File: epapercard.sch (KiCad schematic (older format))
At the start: 47 parts, among them P1 CONN_01X06, P2 A120699CT, Q1 2N7002KW, Q2 BSS84W, Q3 BSS84W, Q4 BSS84W, Q5 2N7002KW, Q6 2N7002KW, Q7 2N7002KW, SW1 SW_PUSH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

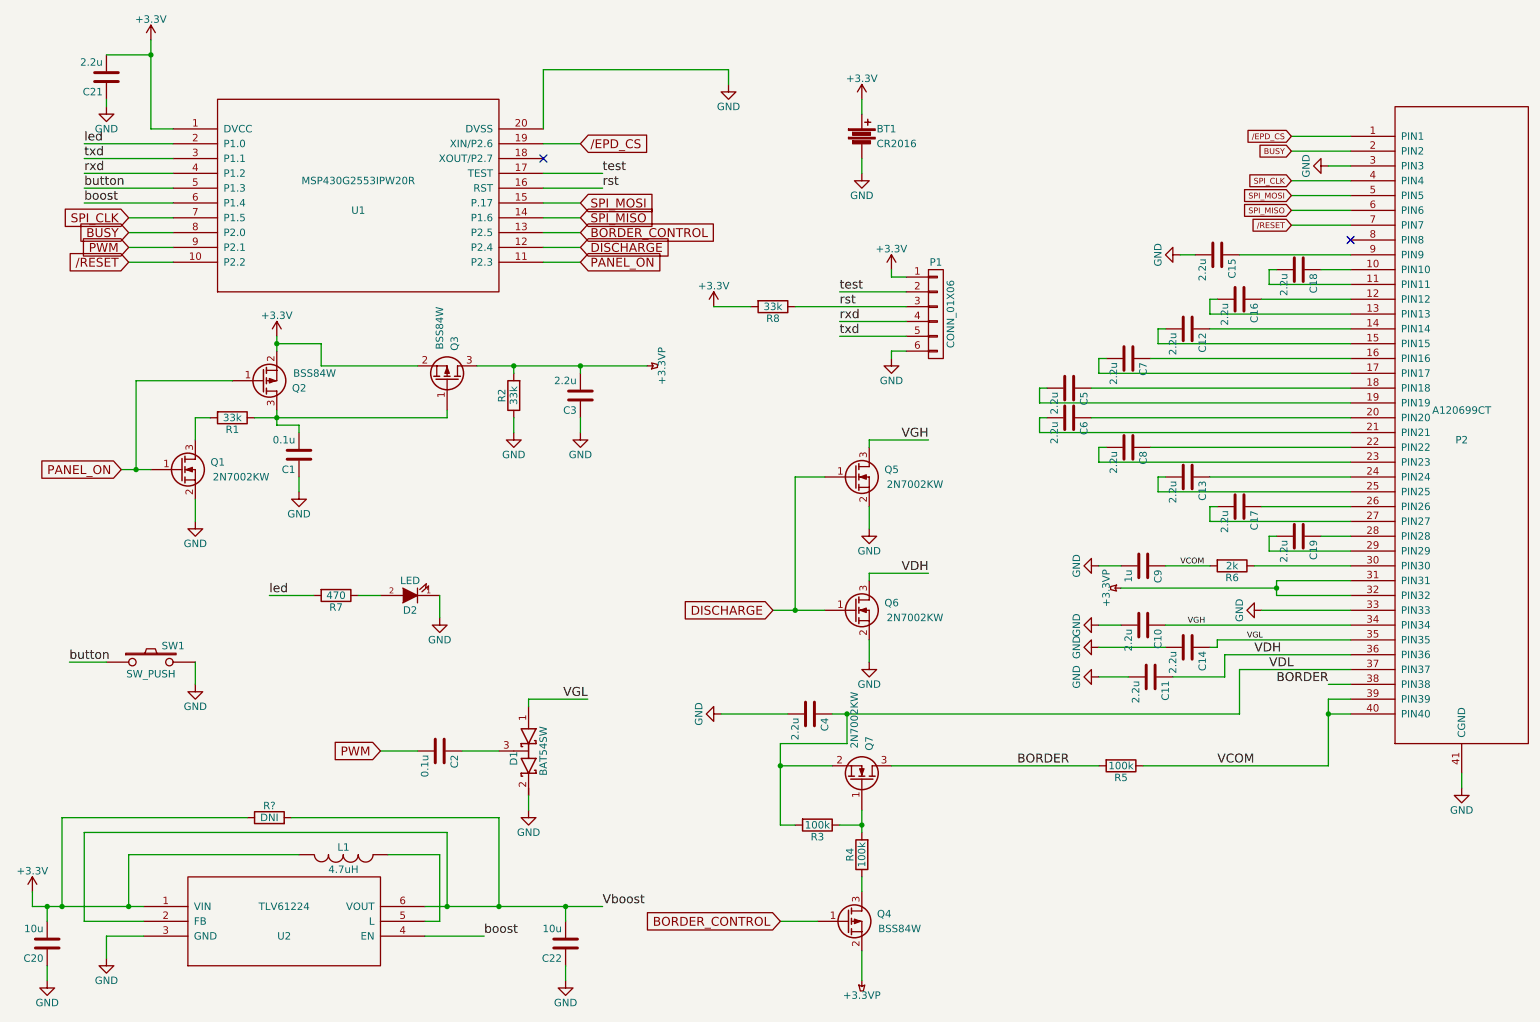
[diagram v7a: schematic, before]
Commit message: Add tabbed battery and boost reg
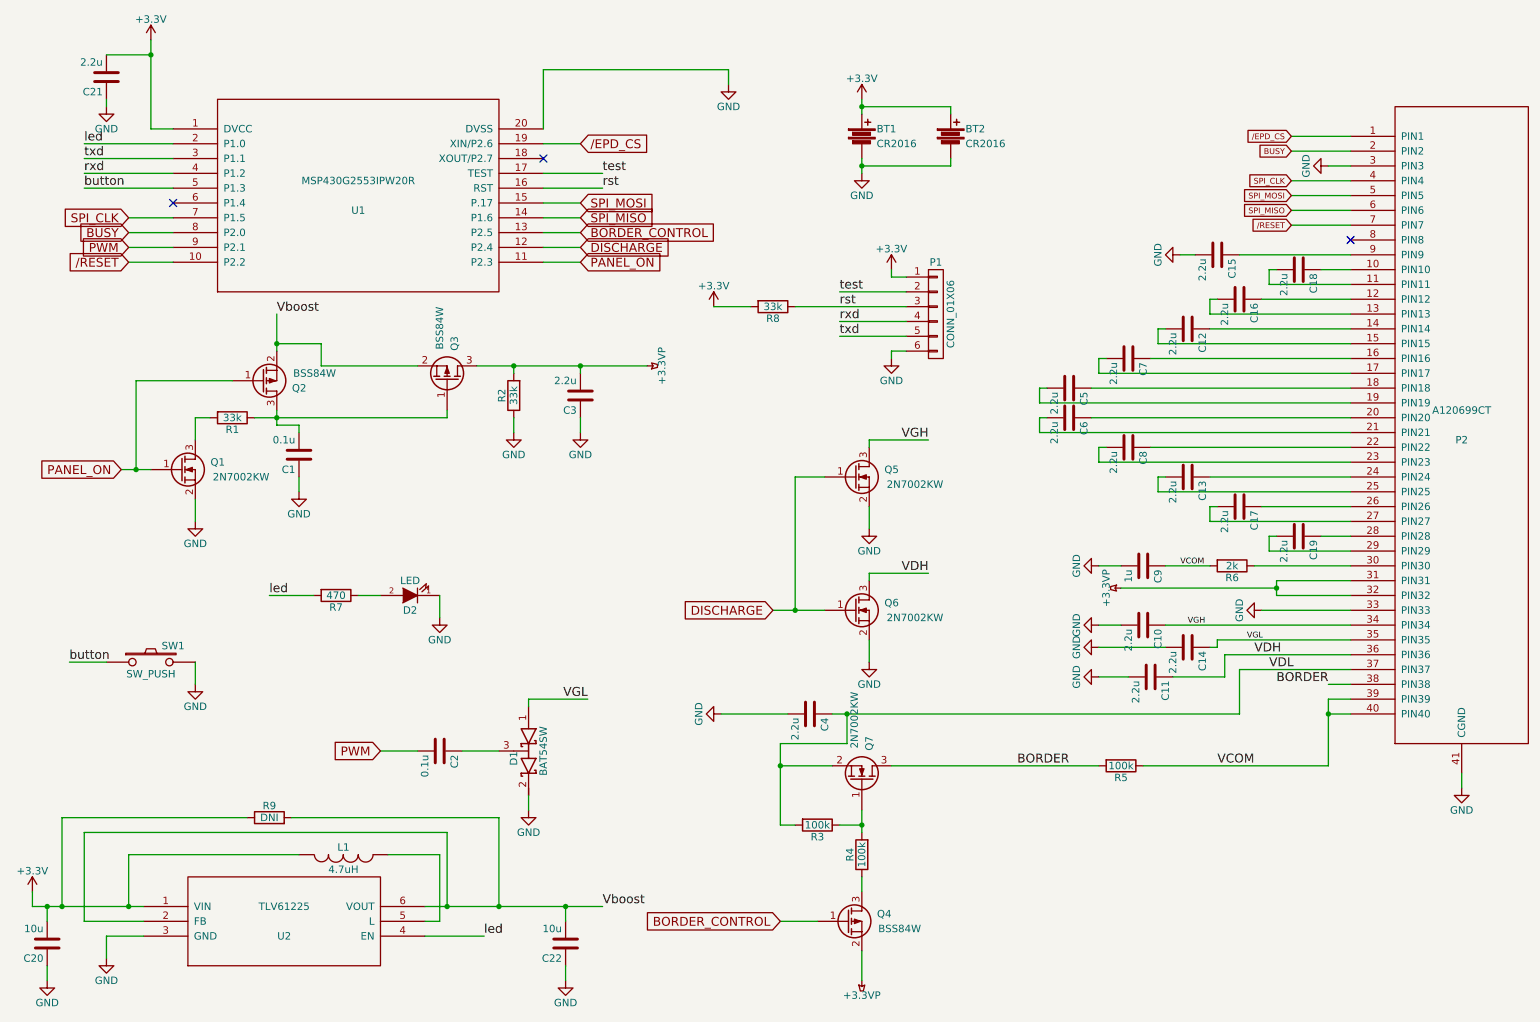
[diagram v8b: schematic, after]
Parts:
- added BT2: CR2016, footprint:CR2032sm, symbol Battery
- BT1: footprint footprint:CR2016sm -> footprint:CR2016sm-F2N
- U2: value TLV61224 -> TLV61225
- gave numbers to parts that had none: 1
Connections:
- net +3V3: now also BT2.1; no longer Q2.2 (S), Q3.2 (S)
- net GND: now also BT2.2
- net Vboost: now also Q2.2 (S), Q3.2 (S)
- net led: now also U2.4 (EN)
- net boost: no longer names the net of U1.6 (P1.4)
- net boost: no longer U2.4 (EN)
- no-connect marks 2 -> 3
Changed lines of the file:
@@
 $EndComp
 $Comp
-L +3.3V #PWR5
+L +3.3V #PWR01
 U 1 1 5733FF8C
 P 1550 700
-F 0 "#PWR5" H 1550 550 50  0001 C CNN
+F 0 "#PWR01" H 1550 550 50  0001 C CNN
 F 1 "+3.3V" H 1550 840 50  0000 C CNN
 F 2 "" H 1550 700 50  0000 C CNN
@@
 $EndComp
 $Comp
-L GND #PWR18
+L GND #PWR02
 U 1 1 5733FFAC
 P 5450 1000
-F 0 "#PWR18" H 5450 750 50  0001 C CNN
+F 0 "#PWR02" H 5450 750 50  0001 C CNN
 F 1 "GND" H 5450 850 50  0000 C CNN
 F 2 "" H 5450 1000 50  0000 C CNN
@@
 $EndComp
 $Comp
-L GND #PWR34
+L GND #PWR03
 U 1 1 57340122
 P 10400 5750
-F 0 "#PWR34" H 10400 5500 50  0001 C CNN
+F 0 "#PWR03" H 10400 5500 50  0001 C CNN
 F 1 "GND" H 10400 5600 50  0000 C CNN
 F 2 "" H 10400 5750 50  0000 C CNN
@@
 BUSY
 $Comp
-L GND #PWR33
+L GND #PWR04
 U 1 1 573405DC
 P 9500 1550
-F 0 "#PWR33" H 9500 1300 50  0001 C CNN
+F 0 "#PWR04" H 9500 1300 50  0001 C CNN
 F 1 "GND" H 9500 1400 50  0000 C CNN
 F 2 "" H 9500 1550 50  0000 C CNN
@@
 $EndComp
 $Comp
-L GND #PWR31
+L GND #PWR05
 U 1 1 57340979
 P 8500 2150
-F 0 "#PWR31" H 8500 1900 50  0001 C CNN
+F 0 "#PWR05" H 8500 1900 50  0001 C CNN
 F 1 "GND" H 8500 2000 50  0000 C CNN
 F 2 "" H 8500 2150 50  0000 C CNN
@@
 $EndComp
 $Comp
-L GND #PWR26
+L GND #PWR06
 U 1 1 5734231E
 P 7950 4250
-F 0 "#PWR26" H 7950 4000 50  0001 C CNN
+F 0 "#PWR06" H 7950 4000 50  0001 C CNN
 F 1 "GND" H 7950 4100 50  0000 C CNN
 F 2 "" H 7950 4250 50  0000 C CNN
@@
 Connection ~ 9150 4400
 $Comp
-L GND #PWR32
+L GND #PWR07
 U 1 1 57342C10
 P 9050 4550
-F 0 "#PWR32" H 9050 4300 50  0001 C CNN
+F 0 "#PWR07" H 9050 4300 50  0001 C CNN
 F 1 "GND" H 9050 4400 50  0000 C CNN
 F 2 "" H 9050 4550 50  0000 C CNN
@@
 VGH
 $Comp
-L GND #PWR27
+L GND #PWR08
 U 1 1 57343007
 P 7950 4650
-F 0 "#PWR27" H 7950 4400 50  0001 C CNN
+F 0 "#PWR08" H 7950 4400 50  0001 C CNN
 F 1 "GND" H 7950 4500 50  0000 C CNN
 F 2 "" H 7950 4650 50  0000 C CNN
@@
 VGL
 $Comp
-L GND #PWR28
+L GND #PWR09
 U 1 1 573432AB
 P 7950 4800
-F 0 "#PWR28" H 7950 4550 50  0001 C CNN
+F 0 "#PWR09" H 7950 4550 50  0001 C CNN
 F 1 "GND" H 7950 4650 50  0000 C CNN
 F 2 "" H 7950 4800 50  0000 C CNN
@@
 	6400 4300 6800 4300
 $Comp
-L GND #PWR22
+L GND #PWR010
 U 1 1 57341714
 P 6400 4000
-F 0 "#PWR22" H 6400 3750 50  0001 C CNN
+F 0 "#PWR010" H 6400 3750 50  0001 C CNN
 F 1 "GND" H 6400 3850 50  0000 C CNN
 F 2 "" H 6400 4000 50  0000 C CNN
@@
 	4100 5150 4500 5150
 $Comp
-L GND #PWR12
+L GND #PWR011
 U 1 1 57343116
 P 4100 5900
-F 0 "#PWR12" H 4100 5650 50  0001 C CNN
+F 0 "#PWR011" H 4100 5650 50  0001 C CNN
 F 1 "GND" H 4100 5750 50  0000 C CNN
 F 2 "" H 4100 5900 50  0000 C CNN
@@
 VDH
 $Comp
-L GND #PWR29
+L GND #PWR012
 U 1 1 57343BAD
 P 7950 5000
-F 0 "#PWR29" H 7950 4750 50  0001 C CNN
+F 0 "#PWR012" H 7950 4750 50  0001 C CNN
 F 1 "GND" H 7950 4850 50  0000 C CNN
 F 2 "" H 7950 5000 50  0000 C CNN
@@
 	8750 4800 8750 4750
 $Comp
-L GND #PWR17
+L GND #PWR013
 U 1 1 57343FFF
 P 5400 5250
-F 0 "#PWR17" H 5400 5000 50  0001 C CNN
+F 0 "#PWR013" H 5400 5000 50  0001 C CNN
 F 1 "GND" H 5400 5100 50  0000 C CNN
 F 2 "" H 5400 5250 50  0000 C CNN
@@
 	6350 6350 6350 6450
 $Comp
-L +3.3VP #PWR30
+L +3.3VP #PWR014
 U 1 1 5734E1DE
 P 8100 4400
-F 0 "#PWR30" H 8250 4350 50  0001 C CNN
+F 0 "#PWR014" H 8250 4350 50  0001 C CNN
 F 1 "+3.3VP" H 8100 4500 50  0000 C CNN
 F 2 "" H 8100 4400 50  0000 C CNN
@@
 $EndComp
 $Comp
-L +3.3VP #PWR21
+L +3.3VP #PWR015
 U 1 1 5734E474
 P 6350 7050
-F 0 "#PWR21" H 6500 7000 50  0001 C CNN
+F 0 "#PWR015" H 6500 7000 50  0001 C CNN
 F 1 "+3.3VP" H 6350 7150 50  0000 C CNN
 F 2 "" H 6350 7050 50  0000 C CNN
@@
 Text GLabel 5800 6650 0    60   Input ~ 0
 BORDER_CONTROL
-$Comp
-L +3.3V #PWR8
-U 1 1 5734EA4E
-P 2400 2700
-F 0 "#PWR8" H 2400 2550 50  0001 C CNN
-F 1 "+3.3V" H 2400 2840 50  0000 C CNN
-F 2 "" H 2400 2700 50  0000 C CNN
-F 3 "" H 2400 2700 50  0000 C CNN
-	1    2400 2700
-	1    0    0    -1
-$EndComp
 $Comp
 L Q_NMOS_GSD Q1
@@
 Connection ~ 1450 3600
 $Comp
-L GND #PWR6
+L GND #PWR017
 U 1 1 5734F778
 P 1850 3950
-F 0 "#PWR6" H 1850 3700 50  0001 C CNN
+F 0 "#PWR017" H 1850 3700 50  0001 C CNN
 F 1 "GND" H 1850 3800 50  0000 C CNN
 F 2 "" H 1850 3950 50  0000 C CNN
@@
 Connection ~ 2400 3250
 $Comp
-L GND #PWR9
+L GND #PWR018
 U 1 1 5735025D
 P 2550 3750
-F 0 "#PWR9" H 2550 3500 50  0001 C CNN
+F 0 "#PWR018" H 2550 3500 50  0001 C CNN
 F 1 "GND" H 2550 3600 50  0000 C CNN
 F 2 "" H 2550 3750 50  0000 C CNN
@@
 	2550 3750 2550 3650
 Wire Wire Line
-	2400 2700 2400 2800
+	2400 2550 2400 2800
 Wire Wire Line
 	3350 2900 2700 2900
@@
 Connection ~ 4450 2900
 $Comp
-L GND #PWR11
+L GND #PWR019
 U 1 1 57350E2E
 P 4000 3350
-F 0 "#PWR11" H 4000 3100 50  0001 C CNN
+F 0 "#PWR019" H 4000 3100 50  0001 C CNN
 F 1 "GND" H 4000 3200 50  0000 C CNN
 F 2 "" H 4000 3350 50  0000 C CNN
@@
 $EndComp
 $Comp
-L GND #PWR14
+L GND #PWR020
 U 1 1 57350EA2
 P 4450 3350
-F 0 "#PWR14" H 4450 3100 50  0001 C CNN
+F 0 "#PWR020" H 4450 3100 50  0001 C CNN
 F 1 "GND" H 4450 3200 50  0000 C CNN
 F 2 "" H 4450 3350 50  0000 C CNN
@@
 	4450 3350 4450 3250
 $Comp
-L +3.3VP #PWR15
+L +3.3VP #PWR021
 U 1 1 57351212
 P 4900 2900
-F 0 "#PWR15" H 5050 2850 50  0001 C CNN
+F 0 "#PWR021" H 5050 2850 50  0001 C CNN
 F 1 "+3.3VP" H 4900 3000 50  0000 C CNN
 F 2 "" H 4900 2900 50  0000 C CNN
@@
 $EndComp
 $Comp
-L GND #PWR23
+L GND #PWR022
 U 1 1 57353B9A
 P 6400 4900
-F 0 "#PWR23" H 6400 4650 50  0001 C CNN
+F 0 "#PWR022" H 6400 4650 50  0001 C CNN
 F 1 "GND" H 6400 4750 50  0000 C CNN
 F 2 "" H 6400 4900 50  0000 C CNN
@@
 button
 $Comp
-L GND #PWR7
+L GND #PWR023
 U 1 1 5735258C
 P 1850 5050
-F 0 "#PWR7" H 1850 4800 50  0001 C CNN
+F 0 "#PWR023" H 1850 4800 50  0001 C CNN
 F 1 "GND" H 1850 4900 50  0000 C CNN
 F 2 "" H 1850 5050 50  0000 C CNN
@@
 $EndComp
 $Comp
-L GND #PWR10
+L GND #PWR024
 U 1 1 5735319E
 P 3500 4600
-F 0 "#PWR10" H 3500 4350 50  0001 C CNN
+F 0 "#PWR024" H 3500 4350 50  0001 C CNN
 F 1 "GND" H 3500 4450 50  0000 C CNN
 F 2 "" H 3500 4600 50  0000 C CNN
@@
 led
 $Comp
-L GND #PWR20
+L GND #PWR025
 U 1 1 57353A35
 P 6350 1600
-F 0 "#PWR20" H 6350 1350 50  0001 C CNN
+F 0 "#PWR025" H 6350 1350 50  0001 C CNN
 F 1 "GND" H 6350 1450 50  0000 C CNN
 F 2 "" H 6350 1600 50  0000 C CNN
@@
 $EndComp
 $Comp
-L +3.3V #PWR19
+L +3.3V #PWR026
 U 1 1 57353E16
 P 6350 1100
-F 0 "#PWR19" H 6350 950 50  0001 C CNN
+F 0 "#PWR026" H 6350 950 50  0001 C CNN
 F 1 "+3.3V" H 6350 1240 50  0000 C CNN
 F 2 "" H 6350 1100 50  0000 C CNN
@@
 $EndComp
 $Comp
-L GND #PWR25
+L GND #PWR027
 U 1 1 57354BED
 P 6550 2850
-F 0 "#PWR25" H 6550 2600 50  0001 C CNN
+F 0 "#PWR027" H 6550 2600 50  0001 C CNN
 F 1 "GND" H 6550 2700 50  0000 C CNN
 F 2 "" H 6550 2850 50  0000 C CNN
@@
 	6550 2800 6650 2800
 $Comp
-L +3.3V #PWR24
+L +3.3V #PWR028
 U 1 1 57354DC5
 P 6550 2250
-F 0 "#PWR24" H 6550 2100 50  0001 C CNN
+F 0 "#PWR028" H 6550 2100 50  0001 C CNN
 F 1 "+3.3V" H 6550 2390 50  0000 C CNN
 F 2 "" H 6550 2250 50  0000 C CNN
@@
 $EndComp
 $Comp
-L +3.3V #PWR16
+L +3.3V #PWR029
 U 1 1 57357D99
 P 5350 2500
-F 0 "#PWR16" H 5350 2350 50  0001 C CNN
+F 0 "#PWR029" H 5350 2350 50  0001 C CNN
 F 1 "+3.3V" H 5350 2640 50  0000 C CNN
 F 2 "" H 5350 2500 50  0000 C CNN
@@
 Connection ~ 1550 800
 $Comp
-L GND #PWR3
+L GND #PWR030
 U 1 1 57358EA6
 P 1250 1150
-F 0 "#PWR3" H 1250 900 50  0001 C CNN
+F 0 "#PWR030" H 1250 900 50  0001 C CNN
 F 1 "GND" H 1250 1000 50  0000 C CNN
 F 2 "" H 1250 1150 50  0000 C CNN
@@
 F 0 "BT1" H 6450 1400 50  0000 L CNN
 F 1 "CR2016" H 6450 1300 50  0000 L CNN
-F 2 "footprint:CR2016sm" V 6350 1390 50  0001 C CNN
+F 2 "footprint:CR2016sm-F2N" V 6350 1390 50  0001 C CNN
 F 3 "" V 6350 1390 50  0000 C CNN
 	1    6350 1350
@@
 P 2450 6650
 F 0 "U2" H 2450 6550 50  0000 C CNN
-F 1 "TLV61224" H 2450 6750 50  0000 C CNN
+F 1 "TLV61225" H 2450 6750 50  0000 C CNN
 F 2 "TO_SOT_Packages_SMD:SOT-23-6_Handsoldering" H 2450 6650 50  0001 C CNN
 F 3 "DOCUMENTATION" H 2450 6650 50  0001 C CNN
@@
 $EndComp
 $Comp
-L +3.3V #PWR1
+L +3.3V #PWR031
 U 1 1 577DEF3F
 P 750 6450
-F 0 "#PWR1" H 750 6300 50  0001 C CNN
+F 0 "#PWR031" H 750 6300 50  0001 C CNN
 F 1 "+3.3V" H 750 6590 50  0000 C CNN
 F 2 "" H 750 6450 50  0000 C CNN
@@
 	750  6550 1500 6550
 $Comp
-L GND #PWR4
+L GND #PWR032
 U 1 1 577DF43A
 P 1250 6900
-F 0 "#PWR4" H 1250 6650 50  0001 C CNN
+F 0 "#PWR032" H 1250 6650 50  0001 C CNN
 F 1 "GND" H 1250 6750 50  0000 C CNN
 F 2 "" H 1250 6900 50  0000 C CNN
@@
 Vboost
 Wire Wire Line
-	1700 1800 1100 1800
-Text Label 1100 1800 0    60   ~ 0
-boost
-Wire Wire Line
 	3400 6750 3800 6750
 Text Label 3800 6750 0    60   ~ 0
-boost
+led
 $Comp
 L C C20
@@
 Connection ~ 4350 6550
 $Comp
-L GND #PWR13
+L GND #PWR033
 U 1 1 577E2C3D
 P 4350 7050
-F 0 "#PWR13" H 4350 6800 50  0001 C CNN
+F 0 "#PWR033" H 4350 6800 50  0001 C CNN
 F 1 "GND" H 4350 6900 50  0000 C CNN
 F 2 "" H 4350 7050 50  0000 C CNN
@@
 $EndComp
 $Comp
-L GND #PWR2
+L GND #PWR034
 U 1 1 577E2D8A
 P 850 7050
-F 0 "#PWR2" H 850 6800 50  0001 C CNN
+F 0 "#PWR034" H 850 6800 50  0001 C CNN
 F 1 "GND" H 850 6900 50  0000 C CNN
 F 2 "" H 850 7050 50  0000 C CNN
@@
 	4350 6950 4350 7050
 $Comp
-L R R?
+L R R9
 U 1 1 577E3E9A
 P 2350 5950
-F 0 "R?" V 2430 5950 50  0000 C CNN
+F 0 "R9" V 2430 5950 50  0000 C CNN
 F 1 "DNI" V 2350 5950 50  0000 C CNN
 F 2 "Resistors_SMD:R_0201" V 2280 5950 50  0001 C CNN
@@
 	3900 5950 3900 6550
 Connection ~ 3900 6550
+NoConn ~ 1700 1800
+$Comp
+L Battery BT2
+U 1 1 5785F1F0
+P 6950 1350
+F 0 "BT2" H 7050 1400 50  0000 L CNN
+F 1 "CR2016" H 7050 1300 50  0000 L CNN
+F 2 "footprint:CR2032sm" V 6950 1390 50  0001 C CNN
+F 3 "" V 6950 1390 50  0000 C CNN
+	1    6950 1350
+	1    0    0    -1
+$EndComp
+Wire Wire Line
+	6950 1200 6950 1150
+Wire Wire Line
+	6950 1150 6350 1150
+Connection ~ 6350 1150
+Wire Wire Line
+	6950 1500 6950 1550
+Wire Wire Line
+	6950 1550 6350 1550
+Connection ~ 6350 1550
+Text Label 2400 2550 0    60   ~ 0
+Vboost
 $EndSCHEMATC
